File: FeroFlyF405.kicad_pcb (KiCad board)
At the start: 4 copper layers, 50 x 65 mm, 154 parts, among them J302 SM04B-GHS-TB(LF)(SN), J601 SM04B-GHS-TB(LF)(SN), J801 SM04B-GHS-TB(LF)(SN), J802 SM06B-GHS-TB(LF)(SN), J803 SM04B-GHS-TB(LF)(SN), J804 SM04B-GHS-TB(LF)(SN), J805 SM06B-GHS-TB(LF)(SN), J901 Conn_01x03_Pin, J902 Conn_01x03_Pin, J903 Conn_01x03_Pin, J904 Conn_01x03_Pin, J905 Conn_01x03_Pin, J906 Conn_01x03_Pin, J907 Conn_01x03_Pin, J908 Conn_01x03_Pin, J909 Conn_01x03_Pin, J910 Conn_01x03_Pin, J911 Conn_01x03_Pin, J912 Conn_01x03_Pin, J913 12402012E212A, J914 SM04B-GHS-TB(LF)(SN), SW301 SW_Push, SW302 SW_Push, U201 AP62200WU-7, U202 TLV75733PDRV, U301 STM32F405RGTx, U501 LSM6DSL, U502 DPS368, U601 SN65HVD230DR, U901 USBLC6-2P6, Y301 24MHz

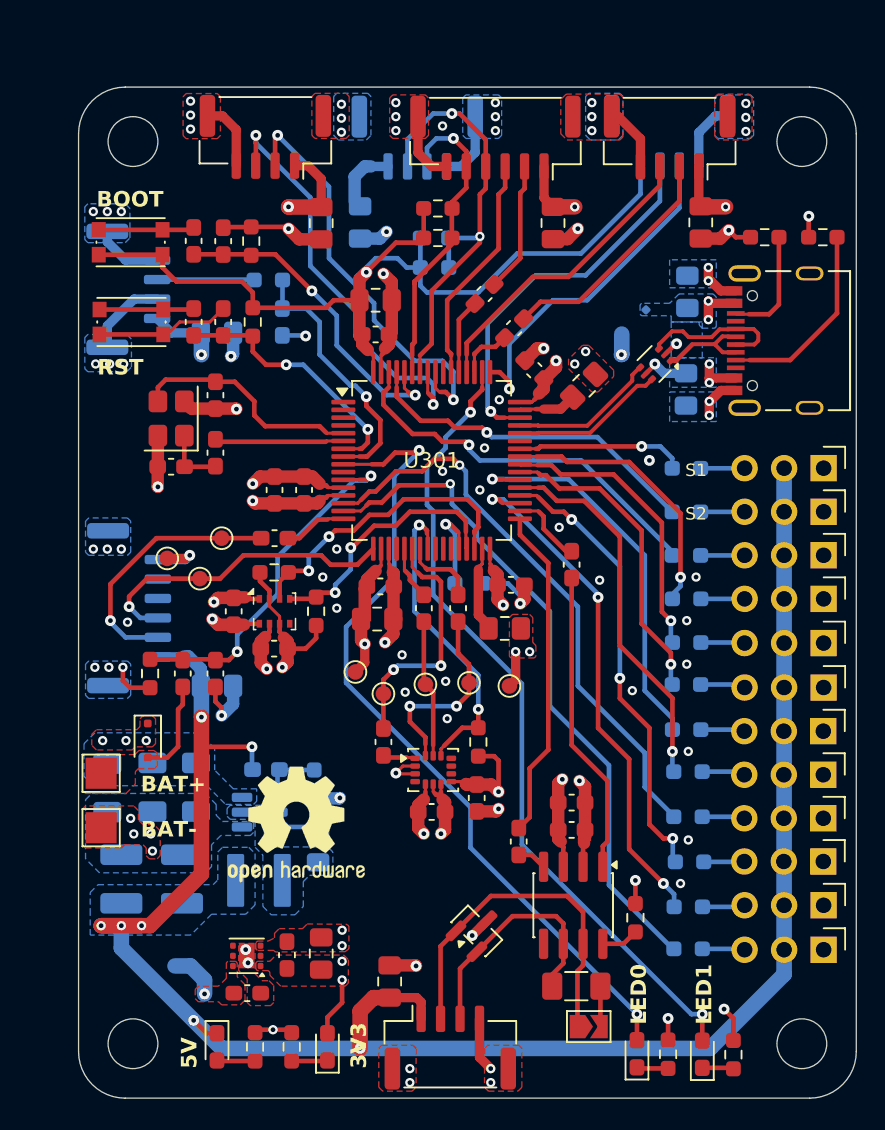
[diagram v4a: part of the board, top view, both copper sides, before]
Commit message: refactor: replace 5V power trace with plane & reposition P_LDOIN trace
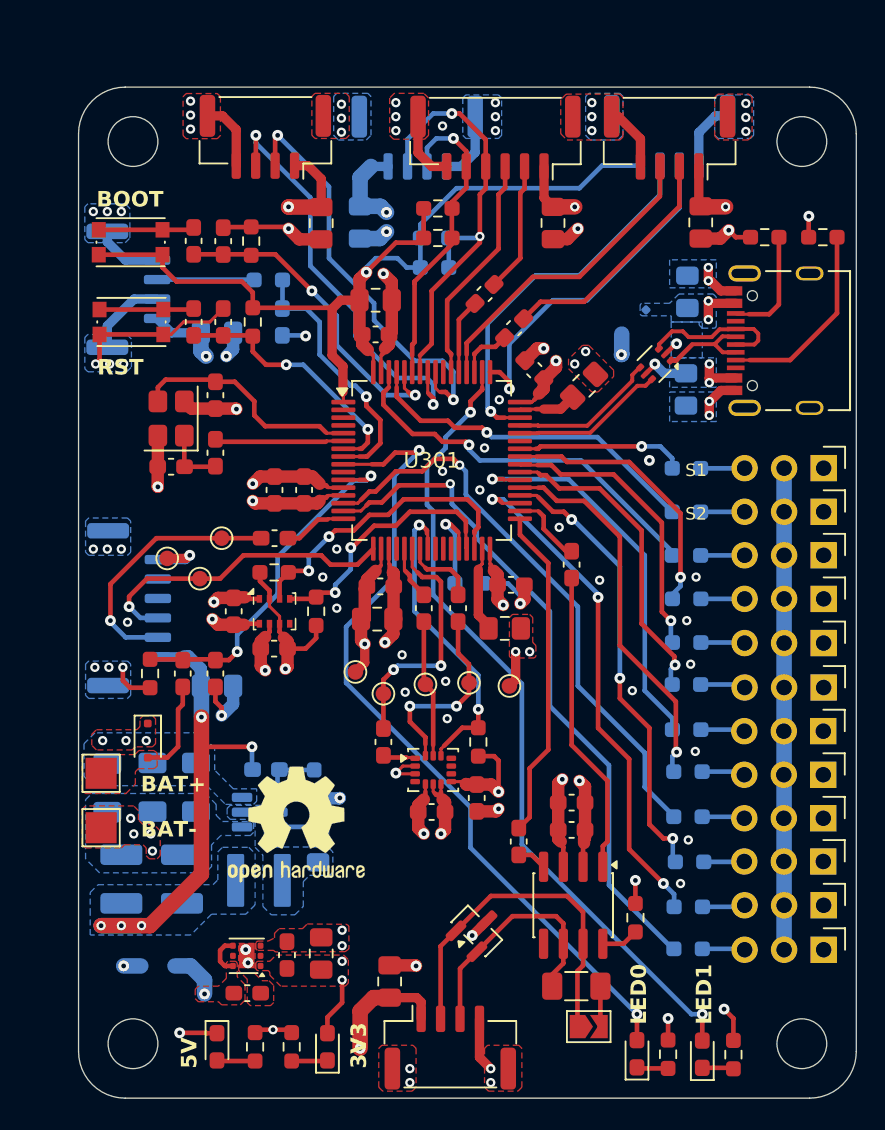
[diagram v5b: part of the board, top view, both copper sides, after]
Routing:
- net +5V: track 206.7 -> 99.3 mm, vias 11 -> 13
- net /IO/P_LDOIN: track 77.8 -> 72.0 mm
- net +3V3: track 227.5 -> 230.8 mm
- net GND: track 148.7 -> 150.9 mm
- added copper zone on In2.Cu, net +5V

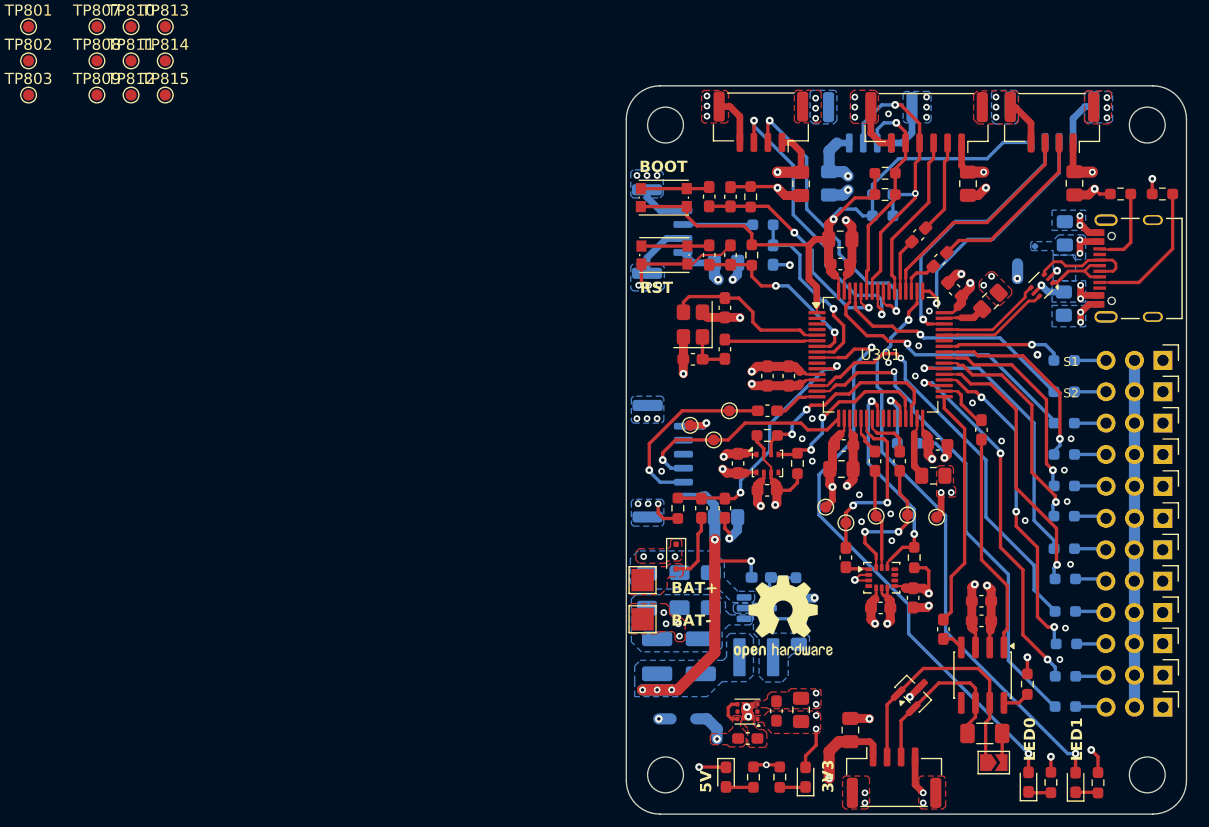
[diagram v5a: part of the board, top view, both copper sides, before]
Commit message: feat: add stiching vias & silkscreen
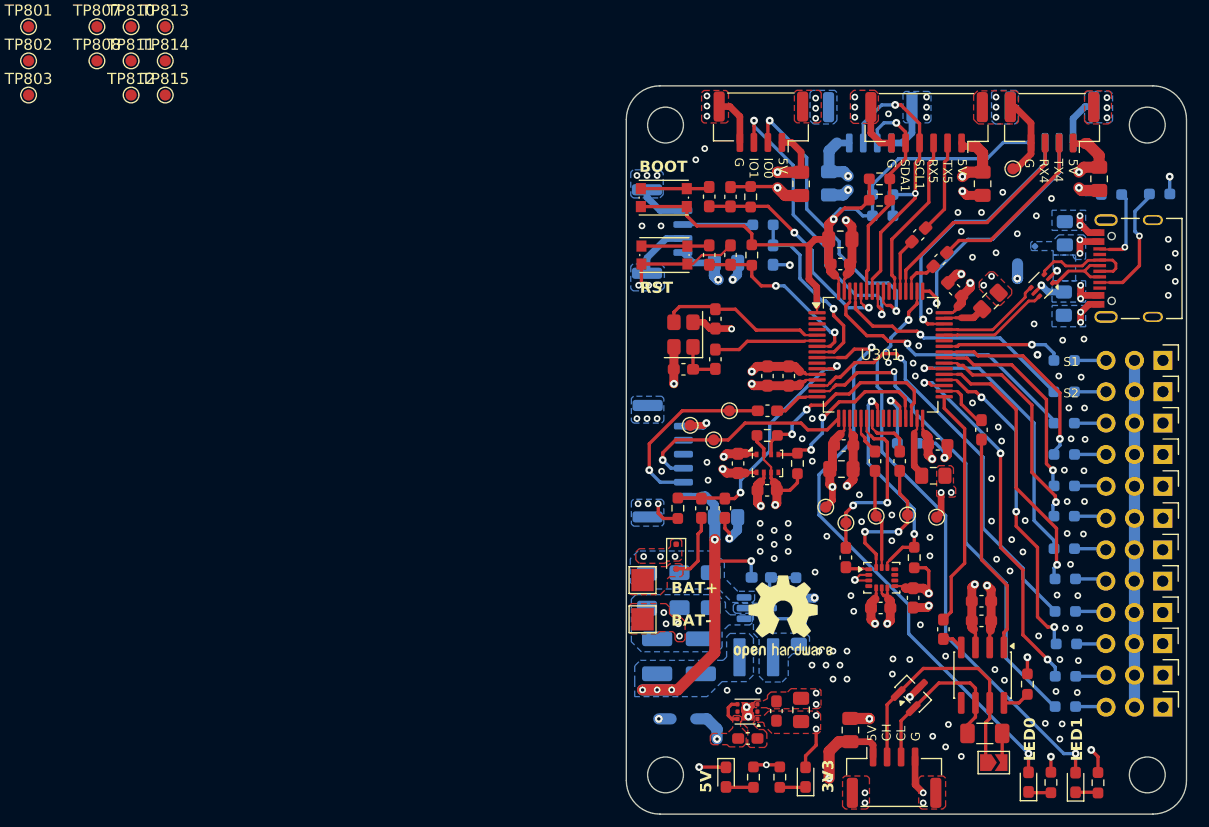
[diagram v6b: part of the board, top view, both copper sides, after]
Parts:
- R901, R902: moved to B.Cu
- moved TP809 82.0 mm to (162.5, 61.4)
- moved C801 2.24 mm to (170.2, 62.3)
- moved C304 1.31 mm to (135.9, 74.8)
- moved C802 1.30 mm to (159.8, 62.7)
- moved R305 1.23 mm to (135.9, 78.4)
- moved C305 1.23 mm to (133.1, 79.3)
- moved Y301 1.23 mm to (133.1, 76.2)
- moved R902 0.81 mm to (171.3, 63.7)
- moved R311 0.71 mm to (150.6, 64.2)
- moved R313 0.71 mm to (150.6, 62.3)
- moved R901 0.25 mm to (175.6, 63.6), turned to 0 degrees
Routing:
- net GND: track 150.9 -> 155.0 mm, vias 103 -> 189
- net +5V: track 99.3 -> 102.6 mm
- net /IO/IO2/D_CC1A: track 12.8 -> 11.3 mm, vias 0 -> 1
- net /MCU/D_OSC_OUT: track 8.16 -> 9.40 mm
- net +3V3: track 230.8 -> 229.9 mm
- net /IO/IO2/D_CC1B: track 7.31 -> 7.18 mm, vias 0 -> 1
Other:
- board text added: "CH"
- board text added: "CL"
- board text added: "CLK"
- board text added: "DIO"
- board text added: "G"
- board text added: "IO0"
- board text added: "IO1"
- board text added: "NC"
- board text added: "RX2"
- board text added: "RX4"
- board text added: "RX5"
- board text added: "SCL1"
- board text added: "SDA1"
- board text added: "TX2"
- board text added: "TX4"
- board text added: "TX5"
